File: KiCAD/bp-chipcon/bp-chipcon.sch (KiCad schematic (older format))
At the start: 34 parts, among them J1 Conn_Coaxial, M1 BLUE_PILL, Q1 2N3904, Q2 2N3906, SW1 power, SW2 A, SW3 UP, SW4 RIGHT, SW5 LEFT, SW6 B, SW7 DOWN, U1 74HC86N

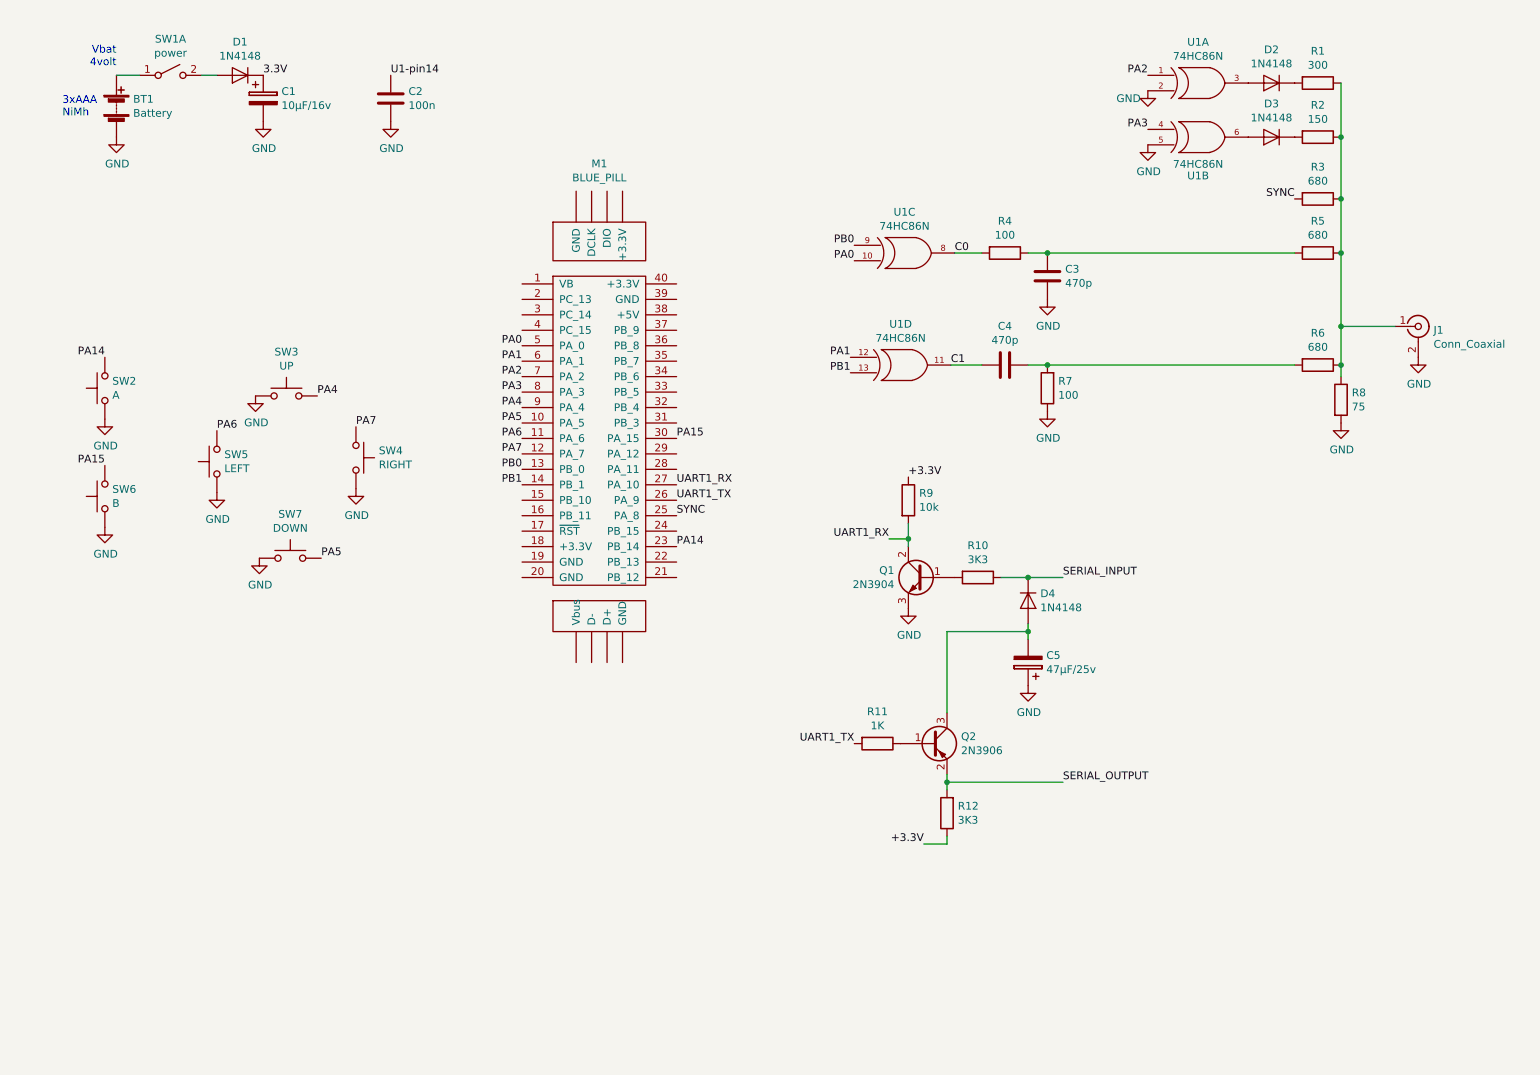
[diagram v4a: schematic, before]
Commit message: added menu and modfications to buttons functions
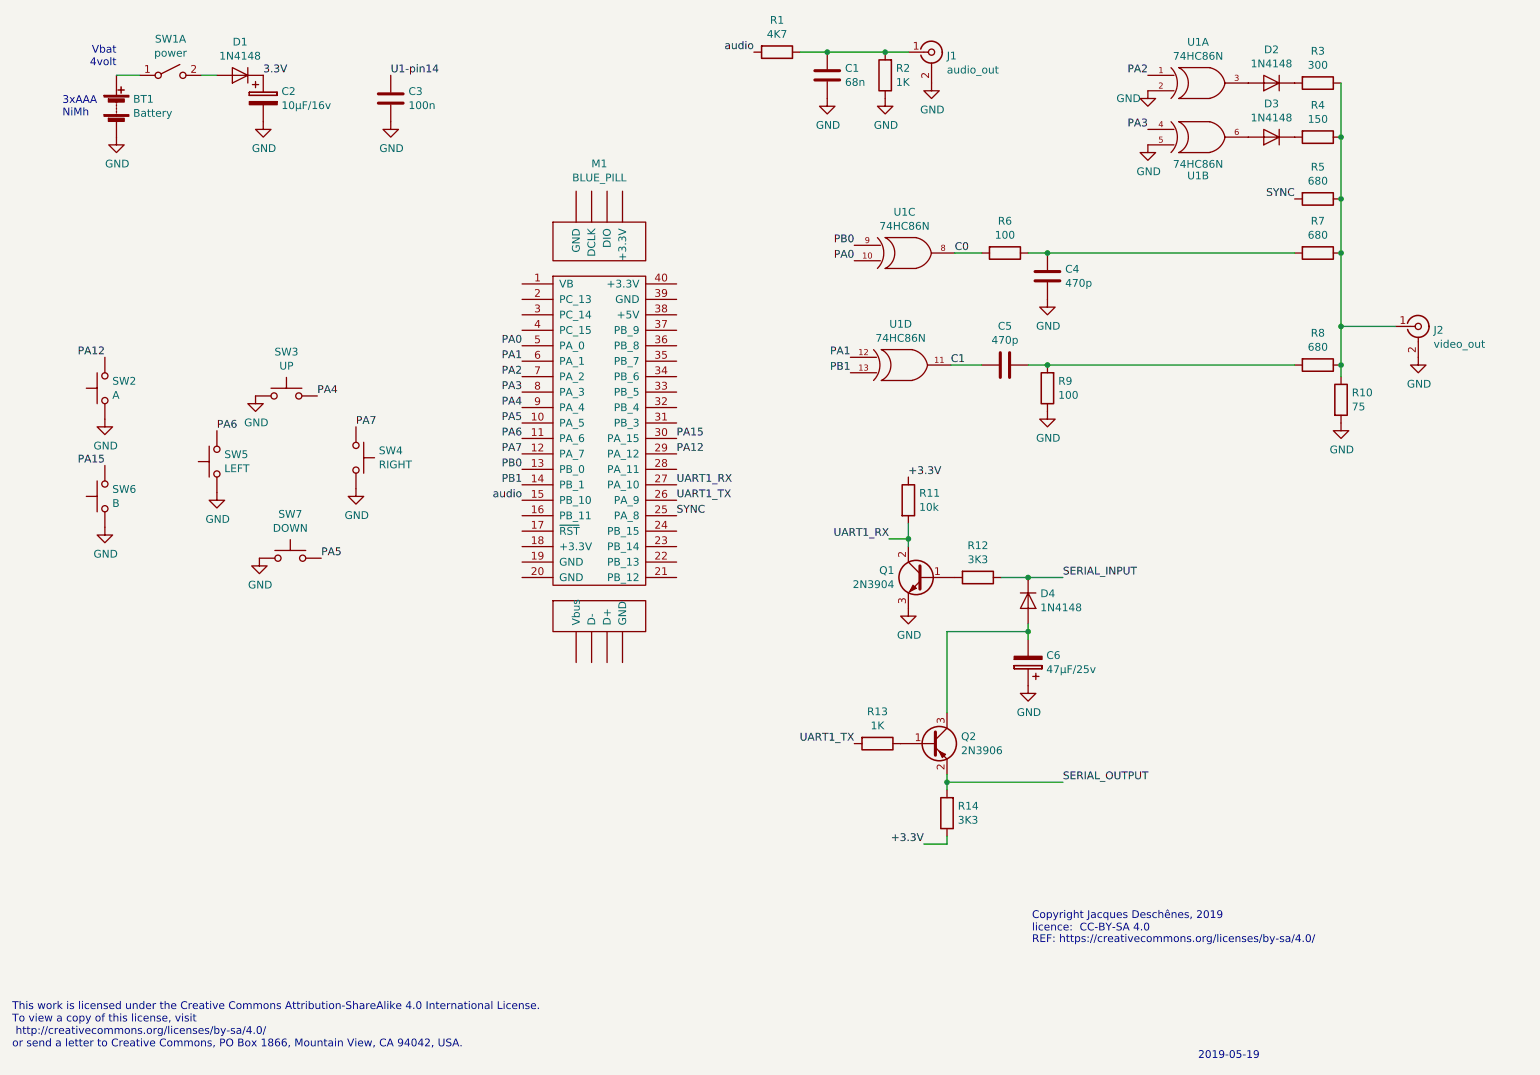
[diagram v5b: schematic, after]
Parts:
- added C1: 68n, symbol device:C
- added J1: audio_out, symbol conn:Conn_Coaxial
- added R1: 4K7, symbol device:R
- added R2: 1K, symbol device:R
- J2: renamed from J1; value Conn_Coaxial -> video_out
- renumbered C1 to C2, C2 to C3, C3 to C4, C4 to C5, C5 to C6, R8 to R10, R9 to R11, R10 to R12, R11 to R13, R12 to R14, R1 to R3, R2 to R4, R3 to R5, R4 to R6, R5 to R7, R6 to R8, R7 to R9
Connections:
- net GND: now also C1.2, J1.2 (Ext), R2.1
- net audio: now reaches M1.15 (PB_10)
- net audio: now also R1.2
- net PA12: now reaches M1.29 (PA_12)
- net PA12: now also SW2.2
- net PA14: no longer names the net of M1.23 (PB_14)
- net PA14: no longer SW2.2
- new net: C1.1, J1.1 (In), R1.1, R2.2
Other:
- note added: "2019-05-19\n"
- note added: "Copyright Jacques Deschênes, 2019\nlicence: CC-BY-SA 4.0"
- note added: "REF: https://creativecommons.org/licenses/by-sa/4.0/"
- note added: "This work is licensed under the Creative Commons Attribution-ShareAlike 4.0 International License.\nTo view a copy of this license, visit\n http://creativecommons.org/licenses/by-sa/4.0/ \nor send a letter to Creative Commons, PO Box 1866, Mountain View, CA 94042, USA."

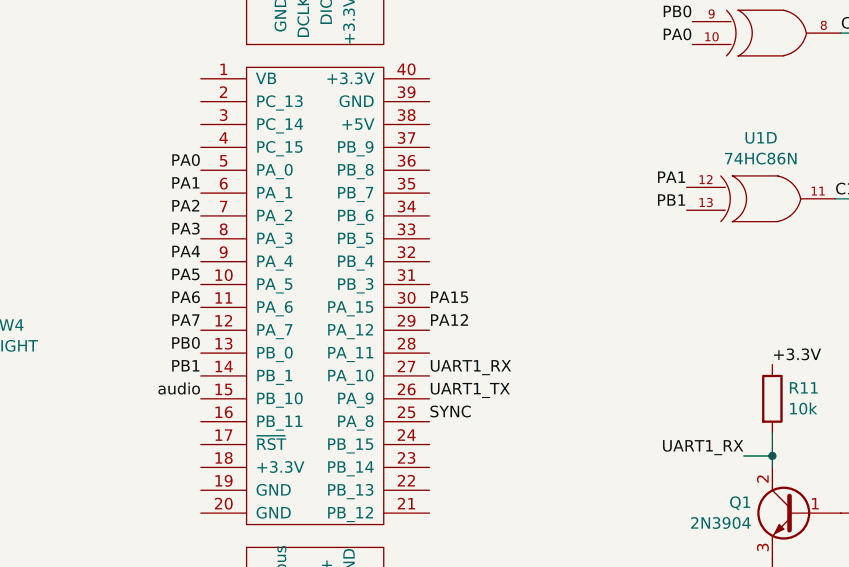
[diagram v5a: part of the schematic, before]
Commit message: modified schematic, eliminated chroma output on PB1. PB0 drive both xor gates. Improved video output pixels size. Pixel width on odd x position were larger than those on even x position. Still trying to reduce scan line jitter.
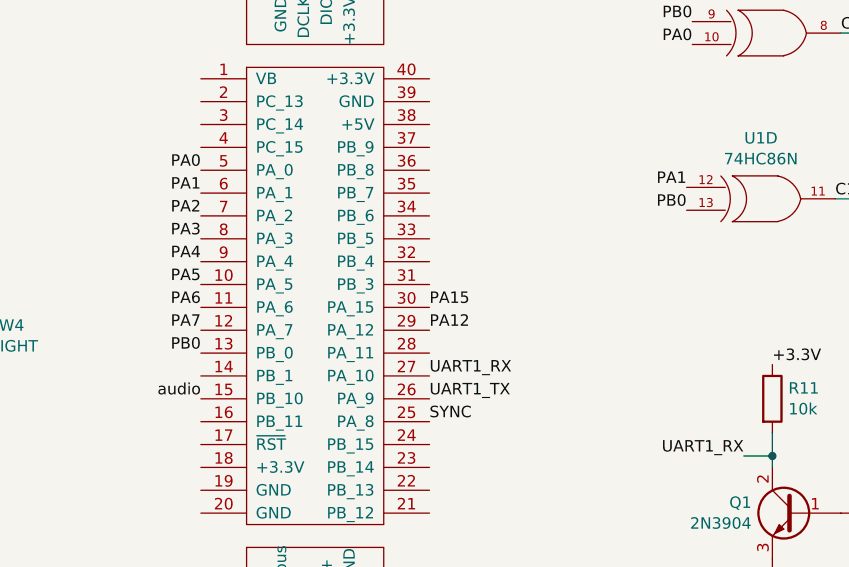
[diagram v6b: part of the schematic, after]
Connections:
- net PB0: now also U1.13
- net PB1: no longer names the net of M1.14 (PB_1)
- net PB1: no longer U1.13
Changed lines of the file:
@@
 Text Label 5975 2350 2    50   ~ 0
 PB0
-Text Label 5950 3175 2    50   ~ 0
-PB1
 Text Label 3825 3800 2    50   ~ 0
 PB0
-Text Label 3825 3900 2    50   ~ 0
-PB1
 Text Label 6625 2400 0    50   ~ 0
 C0
@@
 Text Label 3825 4000 2    50   ~ 0
 audio
+Text Label 5950 3175 2    50   ~ 0
+PB0
 $EndSCHEMATC
